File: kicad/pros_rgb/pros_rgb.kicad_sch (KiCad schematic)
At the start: 41 parts, among them Q73 N54D, U2 20RB, U3 HT32F1654, U5 GD25Q40CT, X1 8MHz

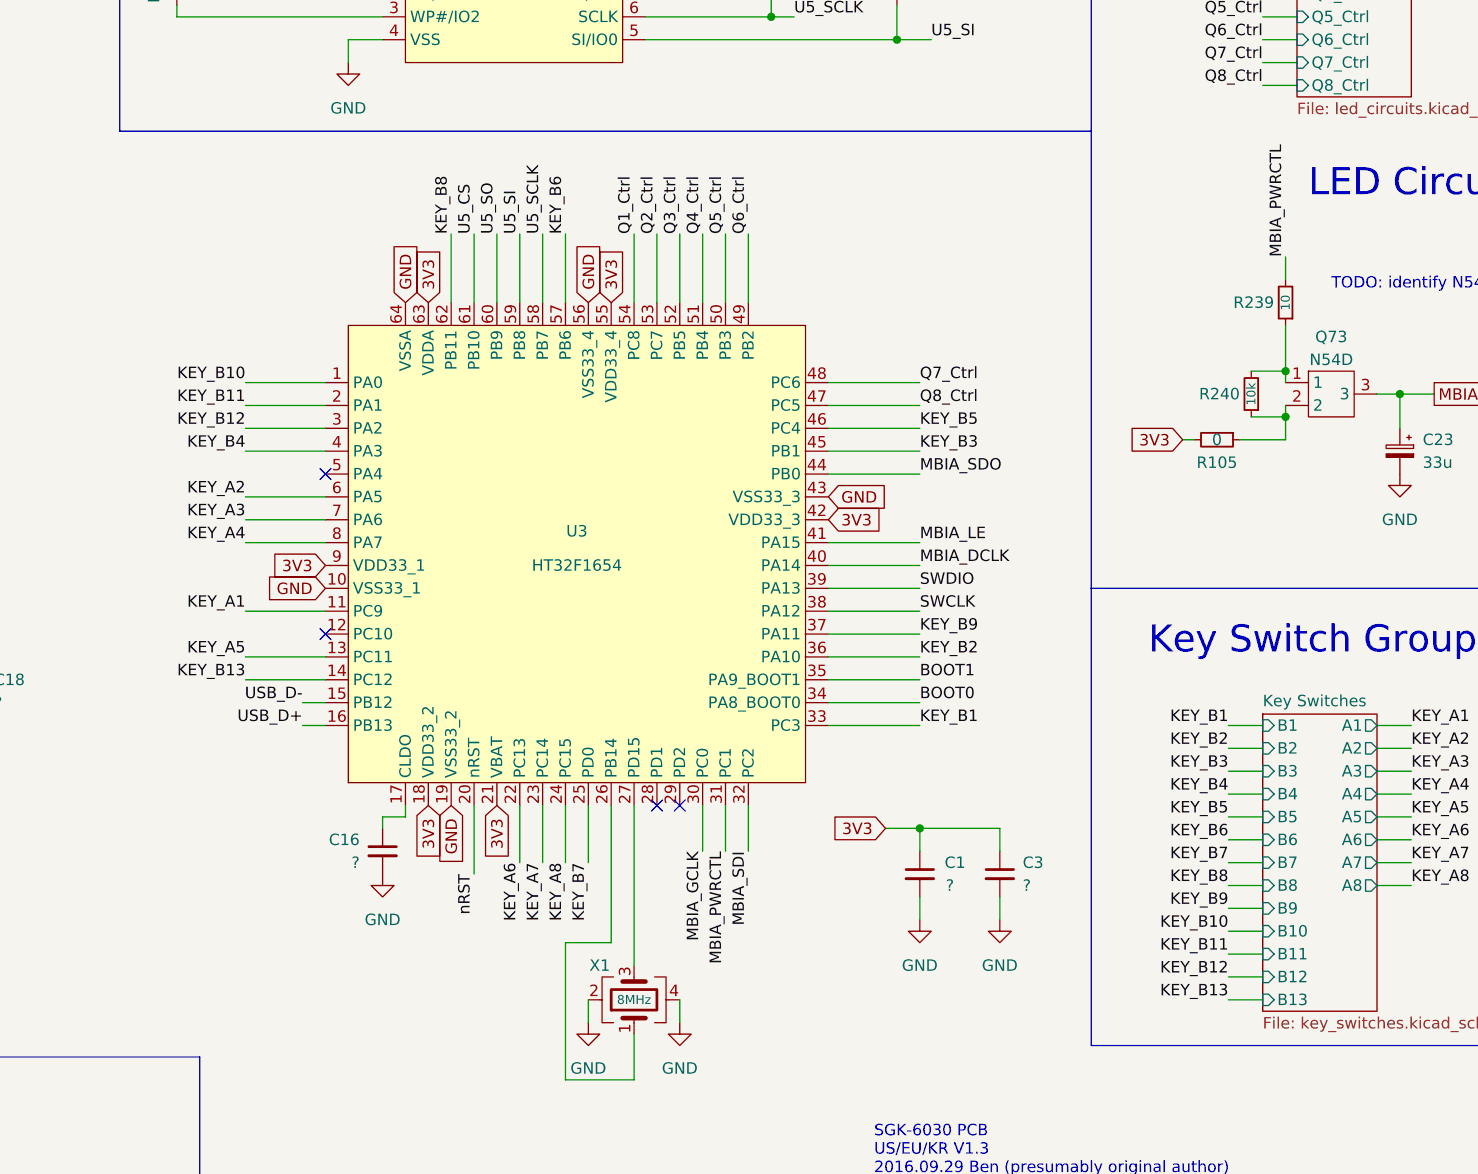
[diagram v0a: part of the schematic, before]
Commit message: kicad/pros_rgb: update key groupings
These new groupings are based off ordering in firmware:
https://github.com/hansemro/pok3r_re_firmware/blob/4b68aa4baf7d28dc8dbf8eebcb1fdb59e7bcd629/disassemble/cmprosrgb/v122/cmprosrgb_v122.txt#L14599-L14629
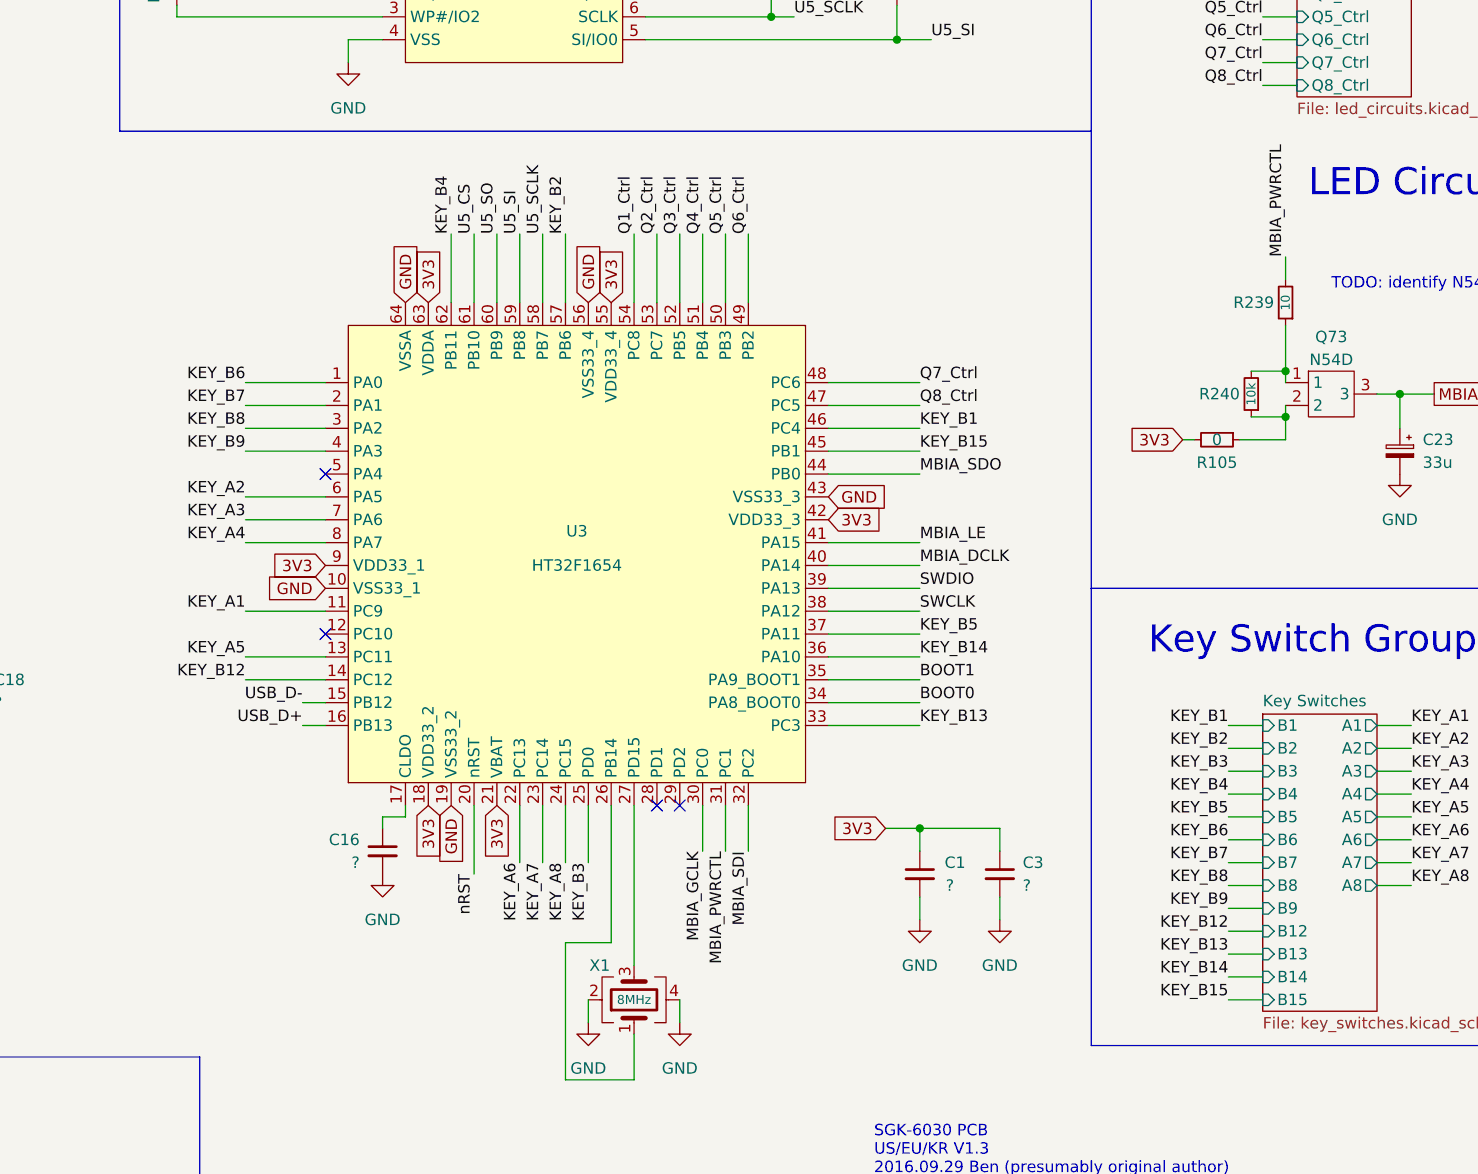
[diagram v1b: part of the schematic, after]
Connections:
- net KEY_B10 is gone; now on net KEY_B6: U3.1 (PA0)
- net KEY_B11 is gone; now on net KEY_B7: U3.2 (PA1)
- net KEY_B1: now also U3.46 (PC4); no longer U3.33 (PC3)
- net KEY_B12: now also U3.14 (PC12); no longer U3.3 (PA2)
- net KEY_B13: now also U3.33 (PC3); no longer U3.14 (PC12)
- net KEY_B2: now also U3.57 (PB6); no longer U3.36 (PA10)
- net KEY_B3: now also U3.25 (PD0); no longer U3.45 (PB1)
- net KEY_B4: now also U3.62 (PB11); no longer U3.4 (PA3)
- net KEY_B5: now also U3.37 (PA11); no longer U3.46 (PC4)
- net KEY_B6: no longer U3.57 (PB6)
- net KEY_B7: no longer U3.25 (PD0)
- net KEY_B8: now also U3.3 (PA2); no longer U3.62 (PB11)
- net KEY_B9: now also U3.4 (PA3); no longer U3.37 (PA11)
- new net KEY_B14: U3.36 (PA10)
- new net KEY_B15: U3.45 (PB1)
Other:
- sheet Key Switches ports: added B14, B15; removed B10, B11
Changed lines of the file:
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@@
     (effects (font (size 1.27 1.27)) (justify left bottom))
   )
-  (label "KEY_B11" (at 109.22 87.63 180)
-    (effects (font (size 1.27 1.27)) (justify right bottom))
-  )
-  (label "KEY_B10" (at 109.22 85.09 180)
-    (effects (font (size 1.27 1.27)) (justify right bottom))
-  )
-  (label "KEY_B8" (at 132.08 68.58 90)
+  (label "KEY_B7" (at 109.22 87.63 180)
+    (effects (font (size 1.27 1.27)) (justify right bottom))
+  )
+  (label "KEY_B6" (at 109.22 85.09 180)
+    (effects (font (size 1.27 1.27)) (justify right bottom))
+  )
+  (label "KEY_B4" (at 132.08 68.58 90)
     (effects (font (size 1.27 1.27)) (justify left bottom))
   )
@@
     (effects (font (size 1.27 1.27)) (justify right bottom))
   )
-  (label "KEY_B3" (at 184.15 92.71 0)
+  (label "KEY_B15" (at 184.15 92.71 0)
     (effects (font (size 1.27 1.27)) (justify left bottom))
   )
@@
     (effects (font (size 1.27 1.27)) (justify left bottom))
   )
-  (label "KEY_B7" (at 147.32 138.43 270)
+  (label "KEY_B3" (at 147.32 138.43 270)
     (effects (font (size 1.27 1.27)) (justify right bottom))
   )
@@
     (effects (font (size 1.27 1.27)) (justify left bottom))
   )
-  (label "KEY_B6" (at 144.78 68.58 90)
+  (label "KEY_B2" (at 144.78 68.58 90)
     (effects (font (size 1.27 1.27)) (justify left bottom))
   )
@@
     (effects (font (size 1.27 1.27)) (justify right bottom))
   )
-  (label "KEY_B11" (at 218.44 148.59 180)
-    (effects (font (size 1.27 1.27)) (justify right bottom))
-  )
-  (label "KEY_B12" (at 218.44 151.13 180)
-    (effects (font (size 1.27 1.27)) (justify right bottom))
-  )
-  (label "KEY_B9" (at 184.15 113.03 0)
+  (label "KEY_B13" (at 218.44 148.59 180)
+    (effects (font (size 1.27 1.27)) (justify right bottom))
+  )
+  (label "KEY_B14" (at 218.44 151.13 180)
+    (effects (font (size 1.27 1.27)) (justify right bottom))
+  )
+  (label "KEY_B5" (at 184.15 113.03 0)
     (effects (font (size 1.27 1.27)) (justify left bottom))
   )
@@
     (effects (font (size 1.27 1.27)) (justify right bottom))
   )
-  (label "KEY_B12" (at 109.22 90.17 180)
+  (label "KEY_B8" (at 109.22 90.17 180)
     (effects (font (size 1.27 1.27)) (justify right bottom))
   )
@@
     (effects (font (size 1.27 1.27)) (justify left bottom))
   )
-  (label "KEY_B13" (at 218.44 153.67 180)
+  (label "KEY_B15" (at 218.44 153.67 180)
     (effects (font (size 1.27 1.27)) (justify right bottom))
   )
@@
     (effects (font (size 1.27 1.27)) (justify right bottom))
   )
-  (label "KEY_B4" (at 109.22 92.71 180)
+  (label "KEY_B9" (at 109.22 92.71 180)
     (effects (font (size 1.27 1.27)) (justify right bottom))
   )
@@
     (effects (font (size 1.27 1.27)) (justify right bottom))
   )
-  (label "KEY_B10" (at 218.44 146.05 180)
-    (effects (font (size 1.27 1.27)) (justify right bottom))
-  )
-  (label "KEY_B2" (at 184.15 115.57 0)
+  (label "KEY_B12" (at 218.44 146.05 180)
+    (effects (font (size 1.27 1.27)) (justify right bottom))
+  )
+  (label "KEY_B14" (at 184.15 115.57 0)
     (effects (font (size 1.27 1.27)) (justify left bottom))
   )
@@
     (effects (font (size 1.27 1.27)) (justify right bottom))
   )
-  (label "KEY_B1" (at 184.15 123.19 0)
+  (label "KEY_B13" (at 184.15 123.19 0)
     (effects (font (size 1.27 1.27)) (justify left bottom))
   )
@@
     (effects (font (size 1.27 1.27)) (justify right bottom))
   )
-  (label "KEY_B13" (at 109.22 118.11 180)
+  (label "KEY_B12" (at 109.22 118.11 180)
     (effects (font (size 1.27 1.27)) (justify right bottom))
   )
@@
     (effects (font (size 1.27 1.27)) (justify left bottom))
   )
-  (label "KEY_B5" (at 184.15 90.17 0)
+  (label "KEY_B1" (at 184.15 90.17 0)
     (effects (font (size 1.27 1.27)) (justify left bottom))
   )
@@
       (effects (font (size 1.27 1.27)) (justify left))
     )
-    (pin "B13" input (at 222.25 153.67 180)
-      (effects (font (size 1.27 1.27)) (justify left))
-    )
-    (pin "B11" input (at 222.25 148.59 180)
-      (effects (font (size 1.27 1.27)) (justify left))
-    )
-    (pin "B12" input (at 222.25 151.13 180)
+    (pin "B15" input (at 222.25 153.67 180)
+      (effects (font (size 1.27 1.27)) (justify left))
+    )
+    (pin "B13" input (at 222.25 148.59 180)
+      (effects (font (size 1.27 1.27)) (justify left))
+    )
+    (pin "B14" input (at 222.25 151.13 180)
       (effects (font (size 1.27 1.27)) (justify left))
     )
@@
       (effects (font (size 1.27 1.27)) (justify left))
     )
-    (pin "B10" input (at 222.25 146.05 180)
-      (effects (font (size 1.27 1.27)) (justify left))
-    )
+    (pin "B12" input (at 222.25 146.05 180)
+      (effects (font (size 1.27 1.27)) (justify left))
+    )

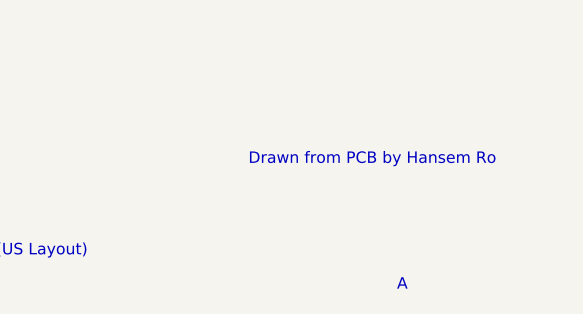
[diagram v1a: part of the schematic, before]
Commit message: kicad/pros_rgb: mark as Rev. B
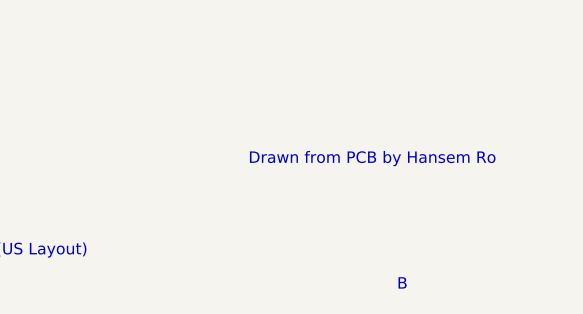
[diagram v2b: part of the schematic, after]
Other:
- note added: "B"
- note removed: "A"
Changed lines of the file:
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@@
     (effects (font (size 3 3)) (justify left bottom))
   )
-  (text "A" (at 269.24 194.31 0)
+  (text "B" (at 269.24 194.31 0)
     (effects (font (size 1.27 1.27)) (justify left bottom))
   )

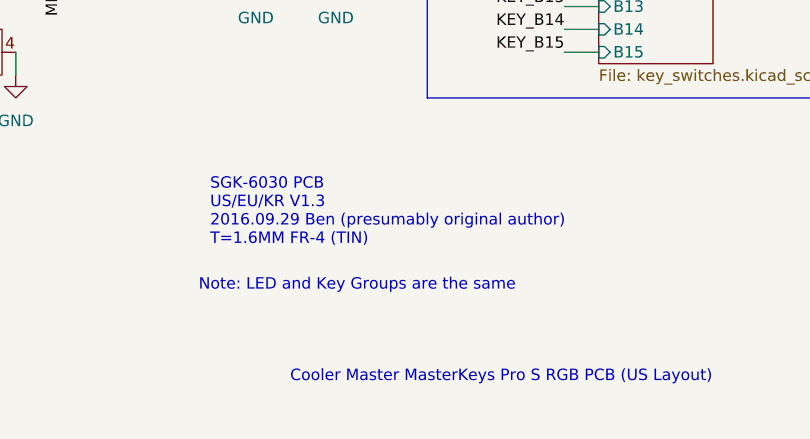
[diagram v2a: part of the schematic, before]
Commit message: kicad/pros_rgb: remove incorrect text statement
Removes invalid statement about key and led groupings being the same.
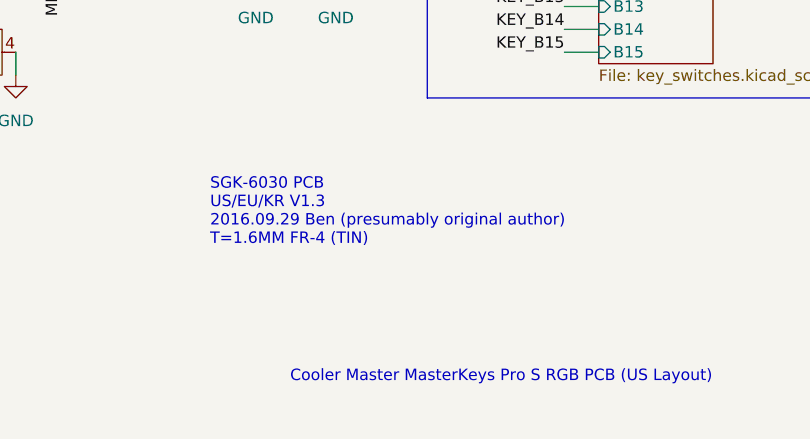
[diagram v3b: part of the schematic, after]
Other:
- note removed: "Note: LED and Key Groups are the same"
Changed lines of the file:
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@@
-    (effects (font (size 1.27 1.27)) (justify left bottom))
-  )
-  (text "Note: LED and Key Groups are the same" (at 177.8 180.34 0)
     (effects (font (size 1.27 1.27)) (justify left bottom))
   )

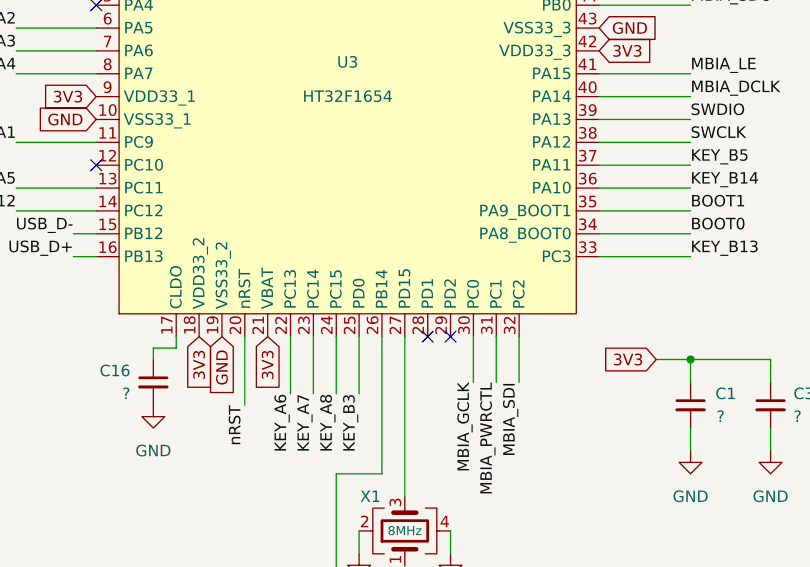
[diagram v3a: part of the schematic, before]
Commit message: kicad/pros_rgb: fix typos
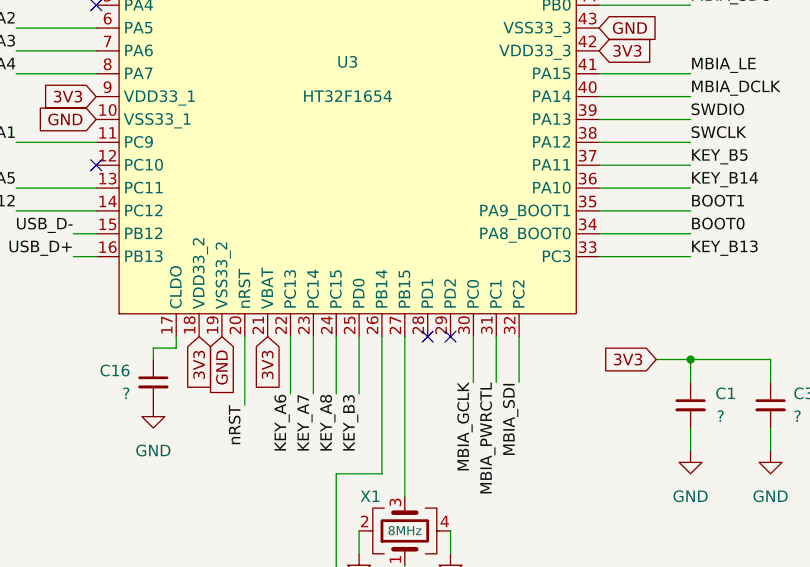
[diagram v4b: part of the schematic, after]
